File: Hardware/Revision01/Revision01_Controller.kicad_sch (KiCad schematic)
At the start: 5 parts, among them U1 NUCLEO-L476RG, U5 STM32WL55CCU6

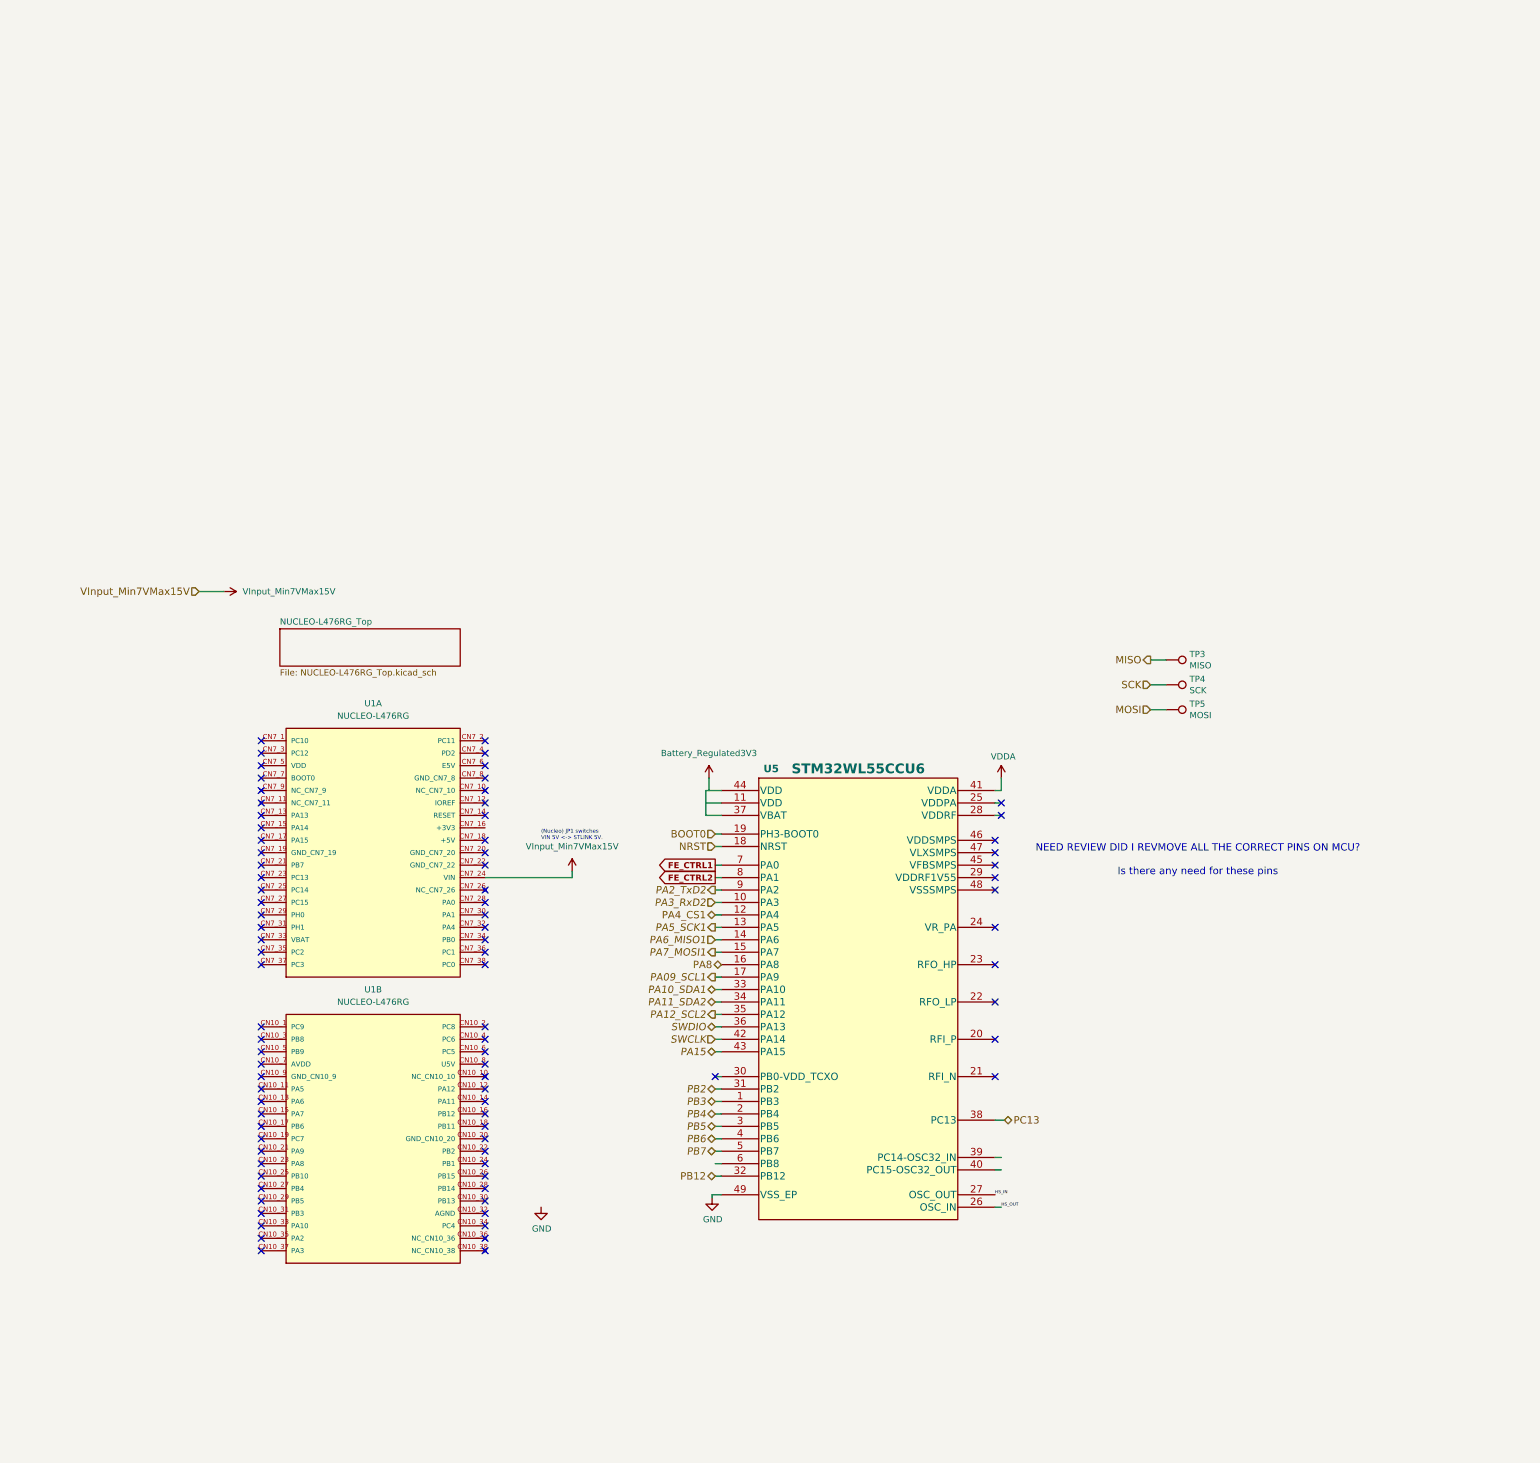
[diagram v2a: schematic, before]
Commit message: . Added local pin labels, ground, and VIN connections for Controller headers. Digital side TODO
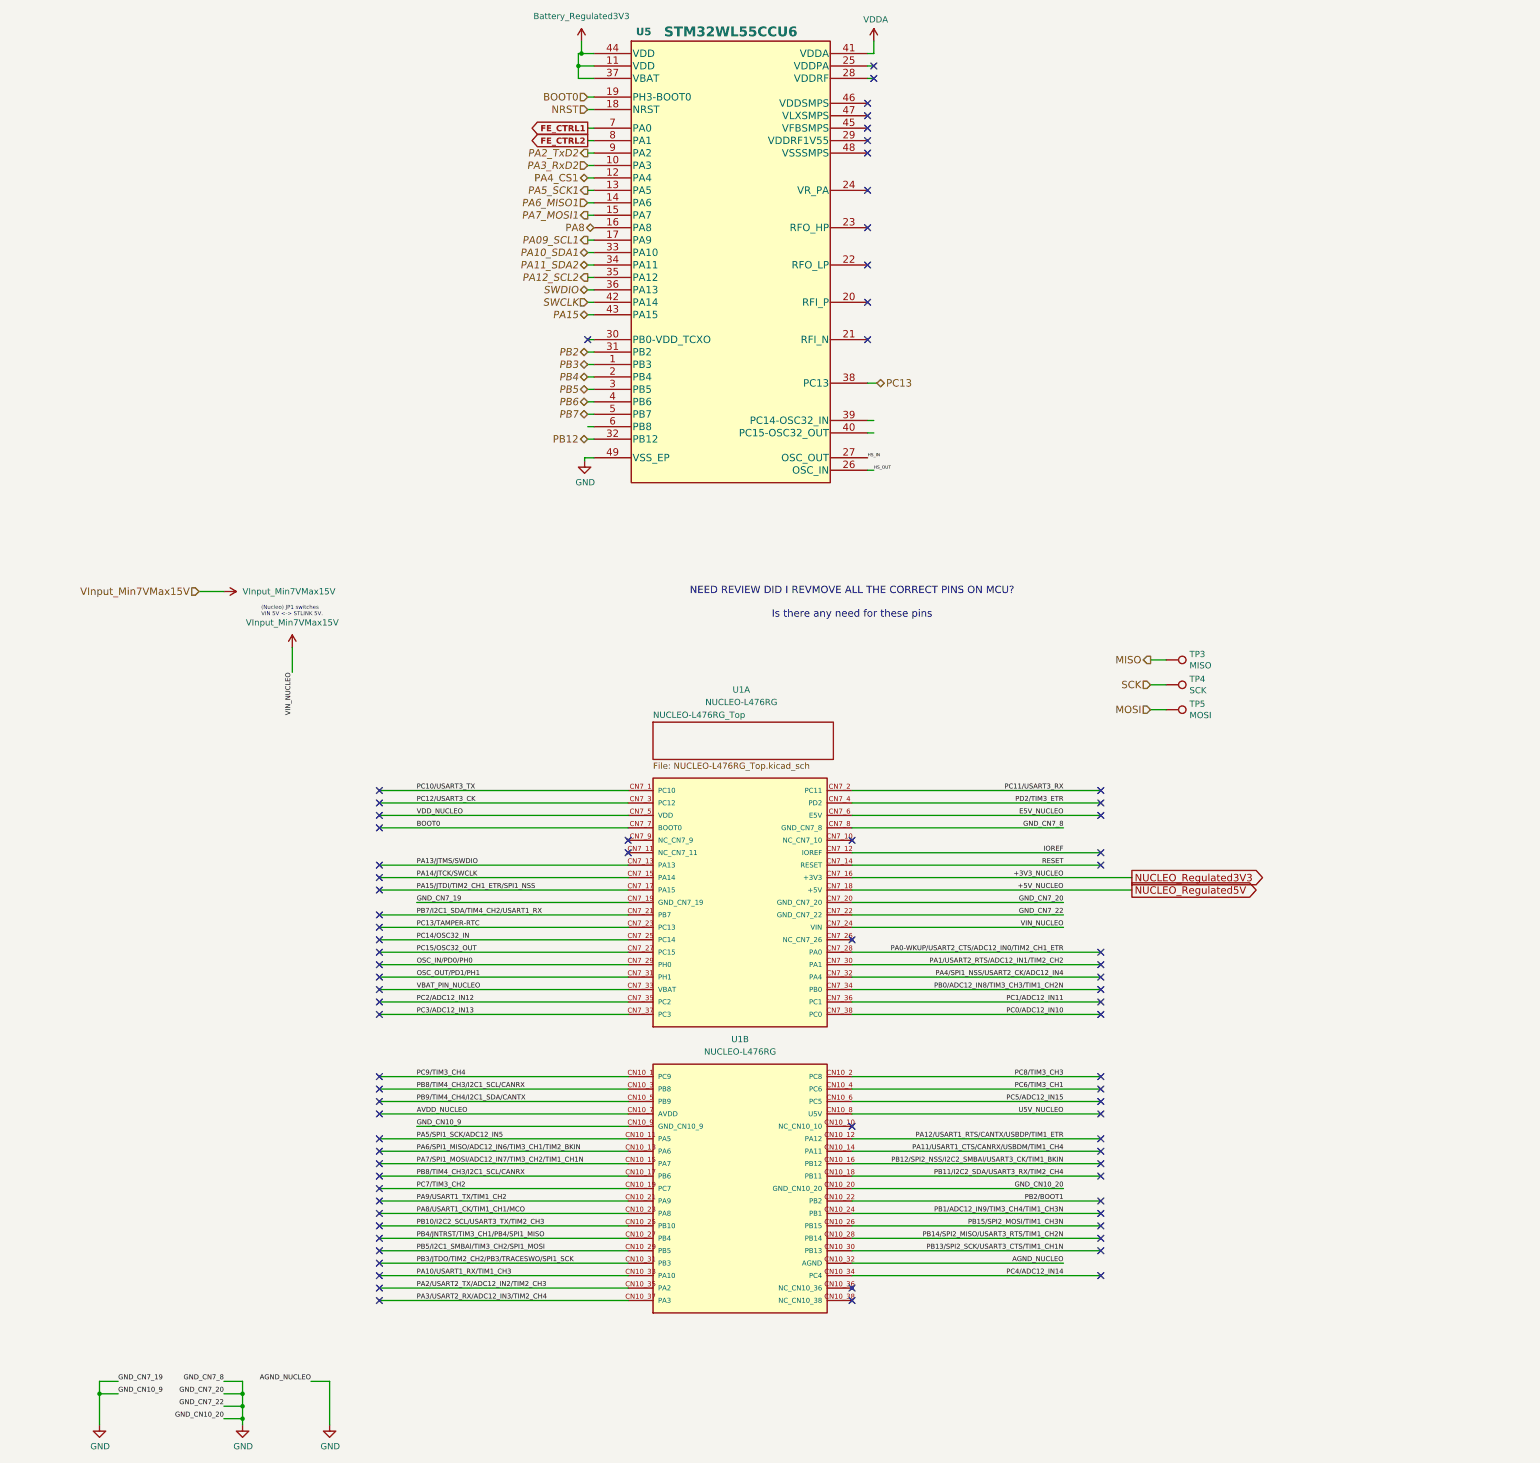
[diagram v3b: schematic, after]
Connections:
- net BOOT0: now also U1.CN7_7 (BOOT0)
- net Battery_Regulated3V3: now also U5.11 (VDD), U5.37 (VBAT), U5.44 (VDD)
- net GND: now also U1.CN10_20 (GND_CN10_20), U1.CN10_32 (AGND), U1.CN10_9 (GND_CN10_9), U1.CN7_19 (GND_CN7_19), U1.CN7_20 (GND_CN7_20), U1.CN7_22 (GND_CN7_22), U1.CN7_8 (GND_CN7_8)
- net PC9/TIM3_CH4: now reaches U1.CN10_1 (PC9)
- net PA5/SPI1_SCK/ADC12_IN5: now reaches U1.CN10_11 (PA5)
- net PA12/USART1_RTS/CANTX/USBDP/TIM1_ETR: now reaches U1.CN10_12 (PA12)
- net PA6/SPI1_MISO/ADC12_IN6/TIM3_CH1/TIM2_BKIN: now reaches U1.CN10_13 (PA6)
- net PA11/USART1_CTS/CANRX/USBDM/TIM1_CH4: now reaches U1.CN10_14 (PA11)
- net PA7/SPI1_MOSI/ADC12_IN7/TIM3_CH2/TIM1_CH1N: now reaches U1.CN10_15 (PA7)
- net PB12/SPI2_NSS/I2C2_SMBAl/USART3_CK/TIM1_BKIN: now reaches U1.CN10_16 (PB12)
- net PB8/TIM4_CH3/I2C1_SCL/CANRX: now reaches U1.CN10_17 (PB6)
- net PB8/TIM4_CH3/I2C1_SCL/CANRX: now also U1.CN10_3 (PB8)
- net PB11/I2C2_SDA/USART3_RX/TIM2_CH4: now reaches U1.CN10_18 (PB11)
- net PC7/TIM3_CH2: now reaches U1.CN10_19 (PC7)
- net PC8/TIM3_CH3: now reaches U1.CN10_2 (PC8)
- net PA9/USART1_TX/TIM1_CH2: now reaches U1.CN10_21 (PA9)
- net PB2/BOOT1: now reaches U1.CN10_22 (PB2)
- net PA8/USART1_CK/TIM1_CH1/MCO: now reaches U1.CN10_23 (PA8)
- net PB1/ADC12_IN9/TIM3_CH4/TIM1_CH3N: now reaches U1.CN10_24 (PB1)
- net PB10/I2C2_SCL/USART3_TX/TIM2_CH3: now reaches U1.CN10_25 (PB10)
- net PB15/SPI2_MOSI/TIM1_CH3N: now reaches U1.CN10_26 (PB15)
- net PB4/JNTRST/TIM3_CH1/PB4/SPI1_MISO: now reaches U1.CN10_27 (PB4)
- net PB14/SPI2_MISO/USART3_RTS/TIM1_CH2N: now reaches U1.CN10_28 (PB14)
- net PB5/I2C1_SMBAl/TIM3_CH2/SPI1_MOSI: now reaches U1.CN10_29 (PB5)
- net PB13/SPI2_SCK/USART3_CTS/TIM1_CH1N: now reaches U1.CN10_30 (PB13)
- net PB3/JTDO/TIM2_CH2/PB3/TRACESWO/SPI1_SCK: now reaches U1.CN10_31 (PB3)
- net PA10/USART1_RX/TIM1_CH3: now reaches U1.CN10_33 (PA10)
- net PC4/ADC12_IN14: now reaches U1.CN10_34 (PC4)
- net PA2/USART2_TX/ADC12_IN2/TIM2_CH3: now reaches U1.CN10_35 (PA2)
- net PA3/USART2_RX/ADC12_IN3/TIM2_CH4: now reaches U1.CN10_37 (PA3)
- net PC6/TIM3_CH1: now reaches U1.CN10_4 (PC6)
- net PB9/TIM4_CH4/I2C1_SDA/CANTX: now reaches U1.CN10_5 (PB9)
- net PC5/ADC12_IN15: now reaches U1.CN10_6 (PC5)
- net AVDD_NUCLEO: now reaches U1.CN10_7 (AVDD)
- net U5V_NUCLEO: now reaches U1.CN10_8 (U5V)
- net PC10/USART3_TX: now reaches U1.CN7_1 (PC10)
- net IOREF: now reaches U1.CN7_12 (IOREF)
- net PA13/JTMS/SWDIO: now reaches U1.CN7_13 (PA13)
- net RESET: now reaches U1.CN7_14 (RESET)
- net PA14/JTCK/SWCLK: now reaches U1.CN7_15 (PA14)
- net NUCLEO_Regulated3V3: now reaches U1.CN7_16 (+3V3)
- net PA15/JTDI/TIM2_CH1_ETR/SPI1_NSS: now reaches U1.CN7_17 (PA15)
- net NUCLEO_Regulated5V: now reaches U1.CN7_18 (+5V)
- net PC11/USART3_RX: now reaches U1.CN7_2 (PC11)
- net PB7/I2C1_SDA/TIM4_CH2/USART1_RX: now reaches U1.CN7_21 (PB7)
- net PC13/TAMPER-RTC: now reaches U1.CN7_23 (PC13)
- net PC14/OSC32_IN: now reaches U1.CN7_25 (PC14)
- net PC15/OSC32_OUT: now reaches U1.CN7_27 (PC15)
- net PA0-WKUP/USART2_CTS/ADC12_IN0/TIM2_CH1_ETR: now reaches U1.CN7_28 (PA0)
- net OSC_IN/PD0/PH0: now reaches U1.CN7_29 (PH0)
- net PC12/USART3_CK: now reaches U1.CN7_3 (PC12)
- net PA1/USART2_RTS/ADC12_IN1/TIM2_CH2: now reaches U1.CN7_30 (PA1)
- net OSC_OUT/PD1/PH1: now reaches U1.CN7_31 (PH1)
- net PA4/SPI1_NSS/USART2_CK/ADC12_IN4: now reaches U1.CN7_32 (PA4)
- net VBAT_PIN_NUCLEO: now reaches U1.CN7_33 (VBAT)
- net PB0/ADC12_IN8/TIM3_CH3/TIM1_CH2N: now reaches U1.CN7_34 (PB0)
- net PC2/ADC12_IN12: now reaches U1.CN7_35 (PC2)
- net PC1/ADC12_IN11: now reaches U1.CN7_36 (PC1)
- net PC3/ADC12_IN13: now reaches U1.CN7_37 (PC3)
- net PC0/ADC12_IN10: now reaches U1.CN7_38 (PC0)
- net PD2/TIM3_ETR: now reaches U1.CN7_4 (PD2)
- net VDD_NUCLEO: now reaches U1.CN7_5 (VDD)
- net E5V_NUCLEO: now reaches U1.CN7_6 (E5V)
- no-connect marks 87 -> 79
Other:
- moved on the sheet: U1A, U1B, U5

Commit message: . Completed MCU schematic & imported hierarchical model pins
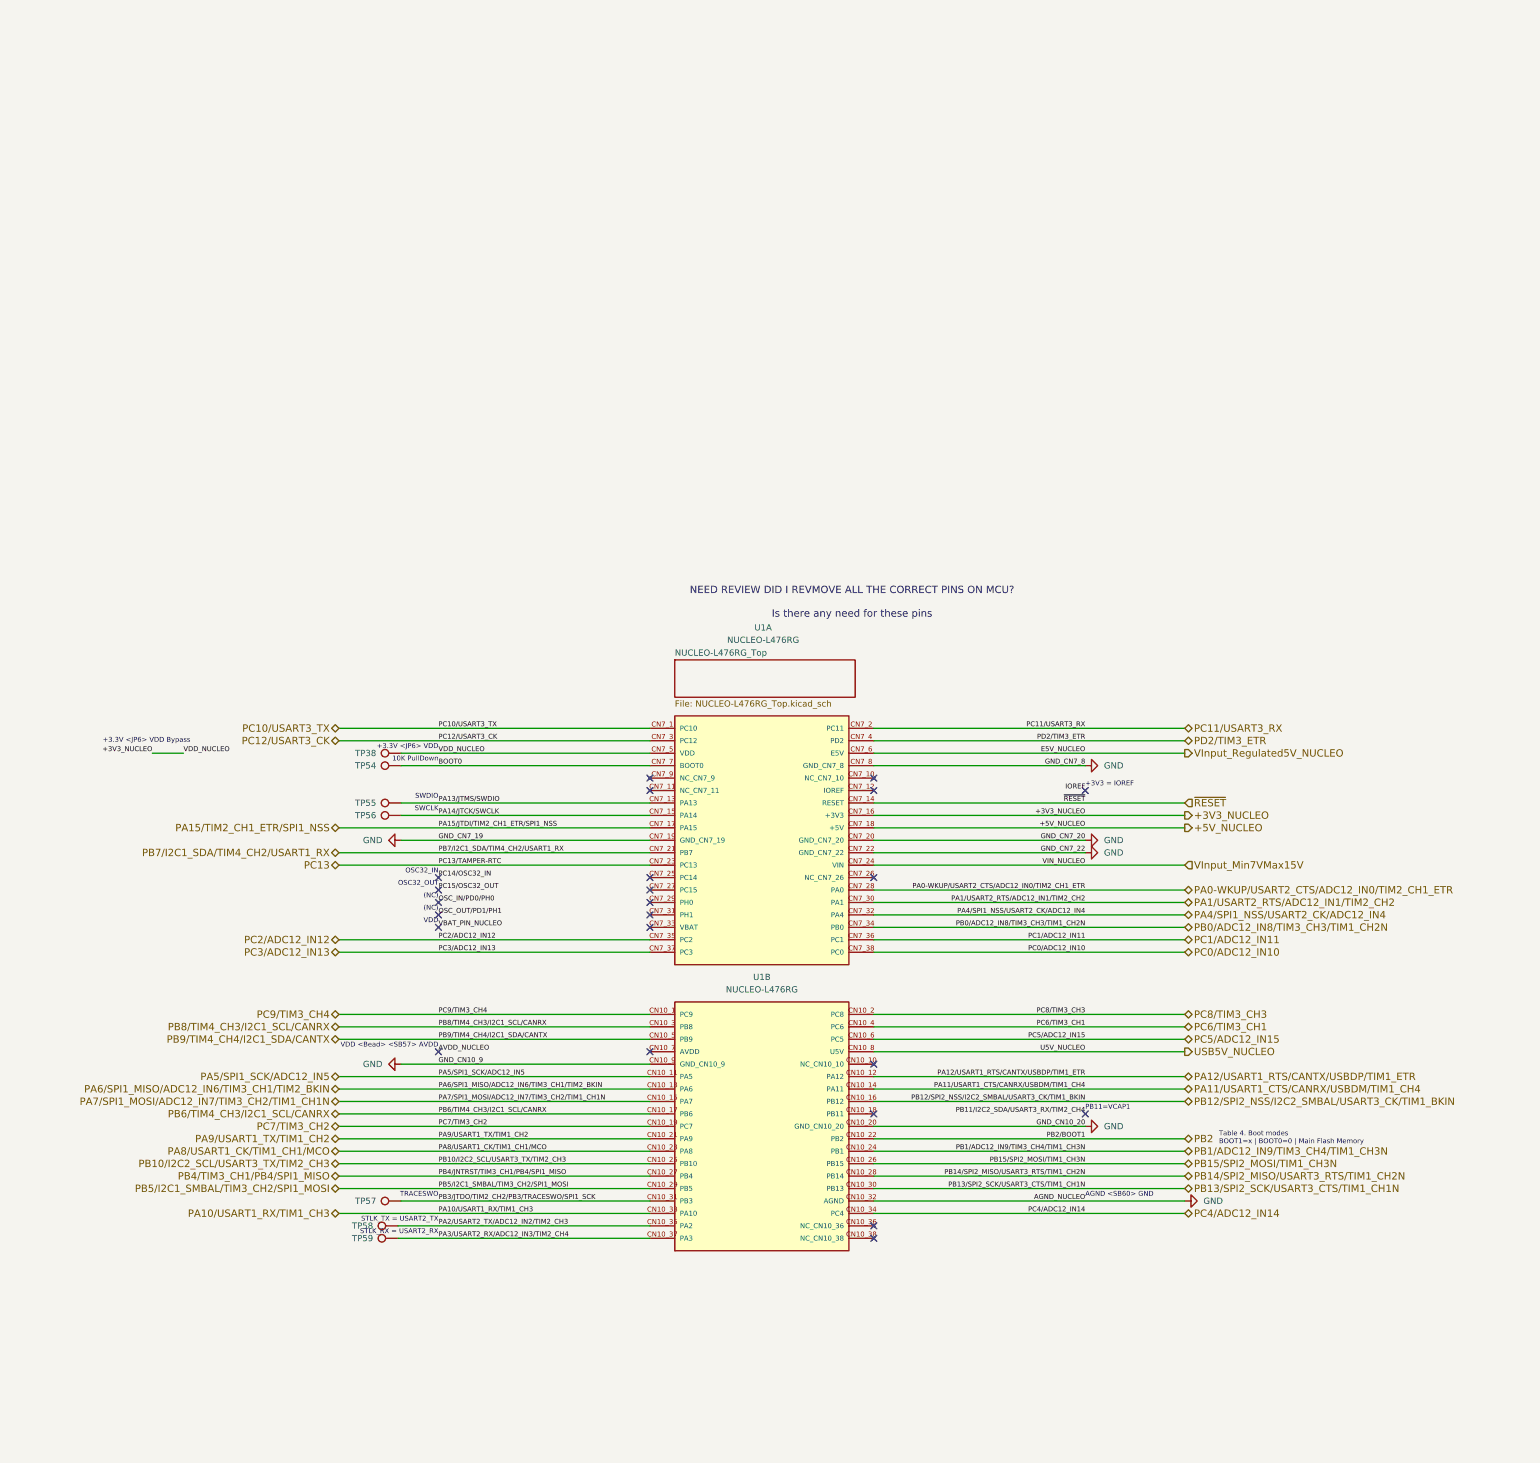
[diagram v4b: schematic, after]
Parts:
- removed TP3: MISO, TestPoint:TestPoint_Pad_D1.5mm, symbol Connector:TestPoint
- removed TP4: SCK, TestPoint:TestPoint_Pad_D1.5mm, symbol Connector:TestPoint
- removed TP5: MOSI, TestPoint:TestPoint_Pad_D1.5mm, symbol Connector:TestPoint
- removed U5: STM32WL55CCU6, Package_DFN_QFN:QFN-48-1EP_7x7mm_P0.5mm_EP5.45x5.45mm, symbol node-lib-v1:STM32WLxx_QFN48
- added TP38, TP54, TP55, TP56, TP57, TP58, TP59: TestPoint, symbol Connector:TestPoint
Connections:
- net PB2/BOOT1 is gone; now on net PB2: U1.CN10_22 (PB2)
- net PC13/TAMPER-RTC is gone; now on net PC13: U1.CN7_23 (PC13)
- net VDD_NUCLEO is gone; now on net +3V3_NUCLEO: U1.CN7_5 (VDD)
- net AVDD_NUCLEO: no longer U1.CN10_7 (AVDD)
- net BOOT0: now also TP54.1
- net IOREF: no longer U1.CN7_12 (IOREF)
- net OSC_IN/PD0/PH0: no longer U1.CN7_29 (PH0)
- net OSC_OUT/PD1/PH1: no longer U1.CN7_31 (PH1)
- net PA13/JTMS/SWDIO: now also TP55.1
- net PA14/JTCK/SWCLK: now also TP56.1
- net PA2/USART2_TX/ADC12_IN2/TIM2_CH3: now also TP58.1
- net PA3/USART2_RX/ADC12_IN3/TIM2_CH4: now also TP59.1
- net PB11/I2C2_SDA/USART3_RX/TIM2_CH4: no longer U1.CN10_18 (PB11)
- net PB3/JTDO/TIM2_CH2/PB3/TRACESWO/SPI1_SCK: now also TP57.1
- net PC14/OSC32_IN: no longer U1.CN7_25 (PC14)
- net PC15/OSC32_OUT: no longer U1.CN7_27 (PC15)
- net VBAT_PIN_NUCLEO: no longer U1.CN7_33 (VBAT)
- net E5V_NUCLEO renamed VInput_Regulated5V_NUCLEO
- net NUCLEO_Regulated3V3 renamed +3V3_NUCLEO
- net +3V3_NUCLEO: now also TP38.1
- net NUCLEO_Regulated5V renamed +5V_NUCLEO
- net PA0-WKUP/USART2_CTS/ADC12_IN0/TIM2_CH1_ETR renamed PA0-WKUP/USART2_CTS/ADC12_IN0/TIM2_CH1_ETR
- net PA1/USART2_RTS/ADC12_IN1/TIM2_CH2 renamed PA1/USART2_RTS/ADC12_IN1/TIM2_CH2
- net PA10/USART1_RX/TIM1_CH3 renamed PA10/USART1_RX/TIM1_CH3
- net PA11/USART1_CTS/CANRX/USBDM/TIM1_CH4 renamed PA11/USART1_CTS/CANRX/USBDM/TIM1_CH4
- net PA12/USART1_RTS/CANTX/USBDP/TIM1_ETR renamed PA12/USART1_RTS/CANTX/USBDP/TIM1_ETR
- net PA15/JTDI/TIM2_CH1_ETR/SPI1_NSS renamed PA15/TIM2_CH1_ETR/SPI1_NSS
- net PA4/SPI1_NSS/USART2_CK/ADC12_IN4 renamed PA4/SPI1_NSS/USART2_CK/ADC12_IN4
- net PA5/SPI1_SCK/ADC12_IN5 renamed PA5/SPI1_SCK/ADC12_IN5
- net PA6/SPI1_MISO/ADC12_IN6/TIM3_CH1/TIM2_BKIN renamed PA6/SPI1_MISO/ADC12_IN6/TIM3_CH1/TIM2_BKIN
- net PA7/SPI1_MOSI/ADC12_IN7/TIM3_CH2/TIM1_CH1N renamed PA7/SPI1_MOSI/ADC12_IN7/TIM3_CH2/TIM1_CH1N
- net PA8/USART1_CK/TIM1_CH1/MCO renamed PA8/USART1_CK/TIM1_CH1/MCO
- net PA9/USART1_TX/TIM1_CH2 renamed PA9/USART1_TX/TIM1_CH2
- net PB0/ADC12_IN8/TIM3_CH3/TIM1_CH2N renamed PB0/ADC12_IN8/TIM3_CH3/TIM1_CH2N
- net PB1/ADC12_IN9/TIM3_CH4/TIM1_CH3N renamed PB1/ADC12_IN9/TIM3_CH4/TIM1_CH3N
- net PB10/I2C2_SCL/USART3_TX/TIM2_CH3 renamed PB10/I2C2_SCL/USART3_TX/TIM2_CH3
- net PB12/SPI2_NSS/I2C2_SMBAl/USART3_CK/TIM1_BKIN renamed PB12/SPI2_NSS/I2C2_SMBAL/USART3_CK/TIM1_BKIN
- net PB13/SPI2_SCK/USART3_CTS/TIM1_CH1N renamed PB13/SPI2_SCK/USART3_CTS/TIM1_CH1N
- net PB14/SPI2_MISO/USART3_RTS/TIM1_CH2N renamed PB14/SPI2_MISO/USART3_RTS/TIM1_CH2N
- net PB15/SPI2_MOSI/TIM1_CH3N renamed PB15/SPI2_MOSI/TIM1_CH3N
- net PB4/JNTRST/TIM3_CH1/PB4/SPI1_MISO renamed PB4/TIM3_CH1/PB4/SPI1_MISO
- net PB5/I2C1_SMBAl/TIM3_CH2/SPI1_MOSI renamed PB5/I2C1_SMBAL/TIM3_CH2/SPI1_MOSI
- net PB7/I2C1_SDA/TIM4_CH2/USART1_RX renamed PB7/I2C1_SDA/TIM4_CH2/USART1_RX
- net PB8/TIM4_CH3/I2C1_SCL/CANRX renamed PB6/TIM4_CH3/I2C1_SCL/CANRX
- net PB6/TIM4_CH3/I2C1_SCL/CANRX: no longer U1.CN10_3 (PB8)
- net PB9/TIM4_CH4/I2C1_SDA/CANTX renamed PB9/TIM4_CH4/I2C1_SDA/CANTX
- net PC0/ADC12_IN10 renamed PC0/ADC12_IN10
- net PC1/ADC12_IN11 renamed PC1/ADC12_IN11
- net PC10/USART3_TX renamed PC10/USART3_TX
- net PC11/USART3_RX renamed PC11/USART3_RX
- net PC12/USART3_CK renamed PC12/USART3_CK
- net PC2/ADC12_IN12 renamed PC2/ADC12_IN12
- net PC3/ADC12_IN13 renamed PC3/ADC12_IN13
- net PC4/ADC12_IN14 renamed PC4/ADC12_IN14
- net PC5/ADC12_IN15 renamed PC5/ADC12_IN15
- net PC6/TIM3_CH1 renamed PC6/TIM3_CH1
- net PC7/TIM3_CH2 renamed PC7/TIM3_CH2
- net PC8/TIM3_CH3 renamed PC8/TIM3_CH3
- net PC9/TIM3_CH4 renamed PC9/TIM3_CH4
- net PD2/TIM3_ETR renamed PD2/TIM3_ETR
- net RESET renamed ~{RESET}
- net U5V_NUCLEO renamed USB5V_NUCLEO
- new net PB8/TIM4_CH3/I2C1_SCL/CANRX: U1.CN10_3 (PB8)
- no-connect marks 79 -> 23
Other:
- note added: "(NC)"
- note added: "+3.3V <JP6> VDD"
- note added: "+3.3V <JP6> VDD Bypass"
- note added: "+3V3 = IOREF"
- note added: "10K PullDown"
- note added: "AGND <SB60> GND"
- note added: "OSC32_IN"
- note added: "OSC32_OUT"
- note added: "PB11=VCAP1"
- note added: "STLK_RX = USART2_RX"
- note added: "STLK_TX = USART2_TX"
- note added: "SWCLK"
- note added: "SWDIO"
- note added: "TRACESWO"
- note added: "Table 4. Boot modes BOOT1=x | BOOT0=0 | Main Flash Memory"
- note added: "VDD"
- note added: "VDD <Bead> <SB57> AVDD"
- note removed: "(Nucleo) JP1 switches VIN 5V <-> STLINK 5V."
- moved on the sheet: U1A, U1B
